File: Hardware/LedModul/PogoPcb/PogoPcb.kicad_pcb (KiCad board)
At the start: 2 copper layers, 19.2 x 19.2 mm, 6 parts, among them J1 Conn_01x01_Pin, J2 Conn_01x01_Pin, J3 Conn_01x01_Pin, J4 Conn_01x01_Pin, J5 Conn_01x01_Pin, J6 Conn_01x01_Pin

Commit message: improvments
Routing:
- net /24V: track 9.30 -> 22.0 mm, vias 8 -> 10
- net /PWM: track 2.88 -> 9.56 mm, vias 8 -> 10
- net /GND: track 2.78 -> 9.30 mm, vias 8 -> 10
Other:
- board text added: "24V"
- board text added: "GND"
- board text added: "PWM"
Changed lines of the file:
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@@
   (gr_rect (start 68.8 122) (end 88 141.2)
     (stroke (width 0.1) (type default)) (fill none) (layer "Edge.Cuts"))
+  (gr_text "24V" (at 77.8 134.62 -90) (layer "B.SilkS")
+    (effects (font (size 1 1) (thickness 0.15)) (justify left bottom mirror))
+  )
+  (gr_text "GND" (at 79.8 134.62 -90) (layer "B.SilkS")
+    (effects (font (size 1 1) (thickness 0.15)) (justify left bottom mirror))
+  )
+  (gr_text "PWM" (at 75.8 134.62 -90) (layer "B.SilkS")
+    (effects (font (size 1 1) (thickness 0.15)) (justify left bottom mirror))
+  )
+  (gr_text "GND" (at 82.15 132.08) (layer "F.SilkS")
+    (effects (font (size 1 1) (thickness 0.15)) (justify left bottom))
+  )
+  (gr_text "24V" (at 76.9 129.54) (layer "F.SilkS")
+    (effects (font (size 1 1) (thickness 0.15)) (justify left bottom))
+  )
+  (gr_text "PWM" (at 71.6 132.08) (layer "F.SilkS")
+    (effects (font (size 1 1) (thickness 0.15)) (justify left bottom))
+  )
+  (segment (start 81.25 134.6) (end 81.55 134.6) (width 0.5) (layer "F.Cu") (net 1))
+  (segment (start 80.4 135.45) (end 80.45 135.4) (width 0.5) (layer "F.Cu") (net 1))
+  (segment (start 80.4 138.6) (end 80.4 135.45) (width 0.5) (layer "F.Cu") (net 1))
+  (segment (start 80.45 135.4) (end 81.25 134.6) (width 0.5) (layer "F.Cu") (net 1))
   (via (at 85.05 136.05) (size 0.8) (drill 0.4) (layers "F.Cu" "B.Cu") (net 1))
   (via (at 82.2 136.1) (size 0.8) (drill 0.4) (layers "F.Cu" "B.Cu") (net 1))
@@
   (via (at 83.6 132.5) (size 0.8) (drill 0.4) (layers "F.Cu" "B.Cu") (net 1))
   (via (at 81.55 134.6) (size 0.8) (drill 0.4) (layers "F.Cu" "B.Cu") (net 1))
+  (via (at 80.4 138.6) (size 0.8) (drill 0.4) (layers "F.Cu" "B.Cu") (net 1))
   (via (at 82.1 133.15) (size 0.8) (drill 0.4) (layers "F.Cu" "B.Cu") (net 1))
+  (via (at 80.45 135.4) (size 0.8) (drill 0.4) (layers "F.Cu" "B.Cu") (net 1))
   (via (at 83.6 136.6) (size 0.8) (drill 0.4) (layers "F.Cu" "B.Cu") (net 1))
   (via (at 85.65 134.5) (size 0.8) (drill 0.4) (layers "F.Cu" "B.Cu") (net 1))
-  (segment (start 80.4 136.9) (end 80.4 135.75) (width 0.5) (layer "B.Cu") (net 1))
-  (segment (start 80.4 135.75) (end 81.55 134.6) (width 0.5) (layer "B.Cu") (net 1))
+  (segment (start 80.45 135.7) (end 80.4 135.75) (width 0.5) (layer "B.Cu") (net 1))
+  (segment (start 80.4 135.75) (end 80.4 136.9) (width 0.5) (layer "B.Cu") (net 1))
+  (segment (start 81.25 134.6) (end 81.55 134.6) (width 0.5) (layer "B.Cu") (net 1))
+  (segment (start 80.45 135.4) (end 81.25 134.6) (width 0.5) (layer "B.Cu") (net 1))
+  (segment (start 80.45 135.4) (end 80.45 135.7) (width 0.5) (layer "B.Cu") (net 1))
+  (segment (start 80.4 136.9) (end 80.4 138.6) (width 0.5) (layer "B.Cu") (net 1))
+  (segment (start 76.4 135.05) (end 75.85 134.5) (width 0.5) (layer "F.Cu") (net 2))
+  (segment (start 76.4 135.35) (end 76.4 135.05) (width 0.5) (layer "F.Cu") (net 2))
+  (segment (start 76.4 138.45) (end 76.4 135.35) (width 0.5) (layer "F.Cu") (net 2))
+  (segment (start 75.85 134.5) (end 75.25 134.5) (width 0.5) (layer "F.Cu") (net 2))
   (via (at 74.65 136.05) (size 0.8) (drill 0.4) (layers "F.Cu" "B.Cu") (net 2))
+  (via (at 76.4 135.35) (size 0.8) (drill 0.4) (layers "F.Cu" "B.Cu") (net 2))
   (via (at 71.7 133.15) (size 0.8) (drill 0.4) (layers "F.Cu" "B.Cu") (net 2))
   (via (at 74.7 133.2) (size 0.8) (drill 0.4) (layers "F.Cu" "B.Cu") (net 2))
@@
   (via (at 71.15 134.6) (size 0.8) (drill 0.4) (layers "F.Cu" "B.Cu") (net 2))
   (via (at 71.8 136.1) (size 0.8) (drill 0.4) (layers "F.Cu" "B.Cu") (net 2))
+  (via (at 76.4 138.45) (size 0.8) (drill 0.4) (layers "F.Cu" "B.Cu") (net 2))
   (via (at 75.25 134.5) (size 0.8) (drill 0.4) (layers "F.Cu" "B.Cu") (net 2))
   (via (at 73.2 132.5) (size 0.8) (drill 0.4) (layers "F.Cu" "B.Cu") (net 2))
-  (segment (start 76.4 135.65) (end 75.25 134.5) (width 0.5) (layer "B.Cu") (net 2))
+  (segment (start 75.85 134.5) (end 75.25 134.5) (width 0.5) (layer "B.Cu") (net 2))
+  (segment (start 76.4 135.05) (end 75.85 134.5) (width 0.5) (layer "B.Cu") (net 2))
+  (segment (start 76.4 135.65) (end 76.4 135.65) (width 0.5) (layer "B.Cu") (net 2))
   (segment (start 76.4 136.9) (end 76.4 135.65) (width 0.5) (layer "B.Cu") (net 2))
+  (segment (start 76.4 135.65) (end 76.4 135.35) (width 0.5) (layer "B.Cu") (net 2))
+  (segment (start 76.4 135.35) (end 76.4 135.05) (width 0.5) (layer "B.Cu") (net 2))
+  (segment (start 76.4 136.9) (end 76.4 138.45) (width 0.5) (layer "B.Cu") (net 2))
+  (segment (start 78.4 138.55) (end 78.4 135.35) (width 0.5) (layer "F.Cu") (net 3))
+  (segment (start 78.4 135.35) (end 78.4 127.6) (width 0.5) (layer "F.Cu") (net 3))
   (via (at 79.9 124.2) (size 0.8) (drill 0.4) (layers "F.Cu" "B.Cu") (net 3))
   (via (at 76.35 125.6) (size 0.8) (drill 0.4) (layers "F.Cu" "B.Cu") (net 3))
+  (via (at 78.4 138.55) (size 0.8) (drill 0.4) (layers "F.Cu" "B.Cu") (net 3))
   (via (at 78.4 127.6) (size 0.8) (drill 0.4) (layers "F.Cu" "B.Cu") (net 3))
   (via (at 80.45 125.5) (size 0.8) (drill 0.4) (layers "F.Cu" "B.Cu") (net 3))
@@
   (via (at 78.4 123.5) (size 0.8) (drill 0.4) (layers "F.Cu" "B.Cu") (net 3))
   (via (at 79.85 127.05) (size 0.8) (drill 0.4) (layers "F.Cu" "B.Cu") (net 3))
+  (via (at 78.4 135.35) (size 0.8) (drill 0.4) (layers "F.Cu" "B.Cu") (net 3))
   (via (at 77 127.1) (size 0.8) (drill 0.4) (layers "F.Cu" "B.Cu") (net 3))
-  (segment (start 78.4 136.9) (end 78.4 127.6) (width 0.5) (layer "B.Cu") (net 3))
+  (segment (start 78.4 138.55) (end 78.4 138.5) (width 0.5) (layer "B.Cu") (net 3))
+  (segment (start 78.4 136.9) (end 78.4 135.35) (width 0.5) (layer "B.Cu") (net 3))
+  (segment (start 78.4 136.9) (end 78.4 138.55) (width 0.5) (layer "B.Cu") (net 3))
+  (segment (start 78.4 135.35) (end 78.4 127.6) (width 0.5) (layer "B.Cu") (net 3))
   (zone (net 3) (net_name "/24V") (layer "F.Cu") (hatch edge 0.5)
     (connect_pads yes (clearance 0.5))

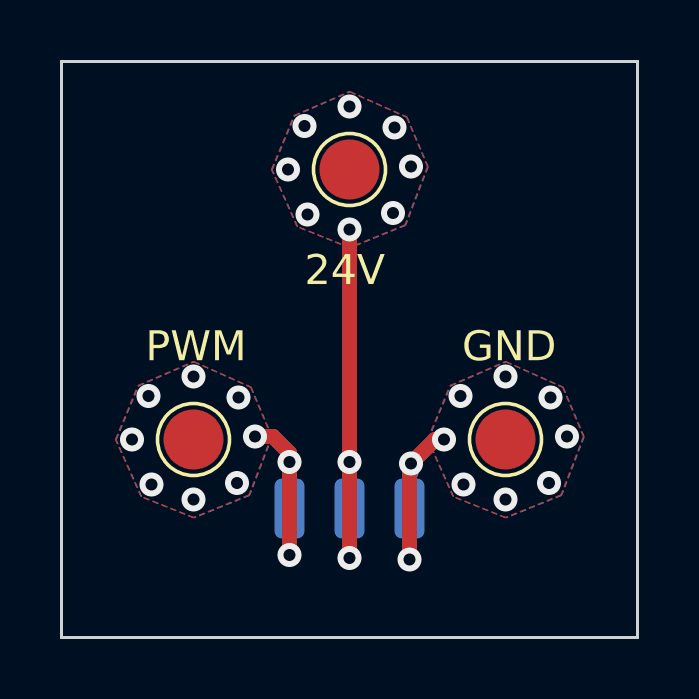
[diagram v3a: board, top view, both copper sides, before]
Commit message: added Pcb name and version to silkscreen
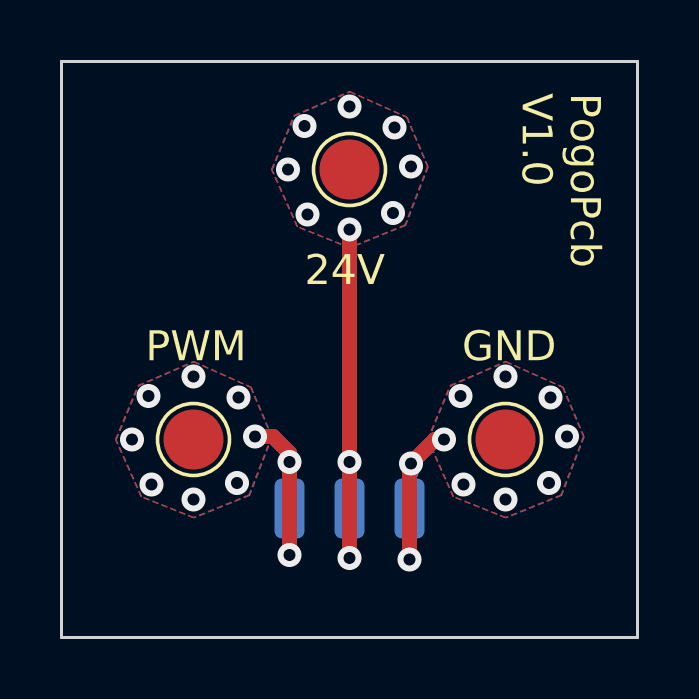
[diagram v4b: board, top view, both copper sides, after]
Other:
- board text added: "PogoPcb V1.0"
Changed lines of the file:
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@@
+    (effects (font (size 1 1) (thickness 0.15)) (justify left bottom mirror))
+  )
+  (gr_text "PogoPcb \nV1.0" (at 84.05 129.65 270) (layer "B.SilkS")
     (effects (font (size 1 1) (thickness 0.15)) (justify left bottom mirror))
   )
@@
     (effects (font (size 1 1) (thickness 0.15)) (justify left bottom))
   )
+  (gr_text "PogoPcb \nV1.0" (at 84.05 123.05 270) (layer "F.SilkS")
+    (effects (font (size 1 1) (thickness 0.15)) (justify left bottom))
+  )
